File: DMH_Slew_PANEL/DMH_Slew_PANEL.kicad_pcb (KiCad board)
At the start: 2 copper layers, 50 x 200 mm, 5 parts, among them J0 Panel_GND_Solder_Wire_Pad

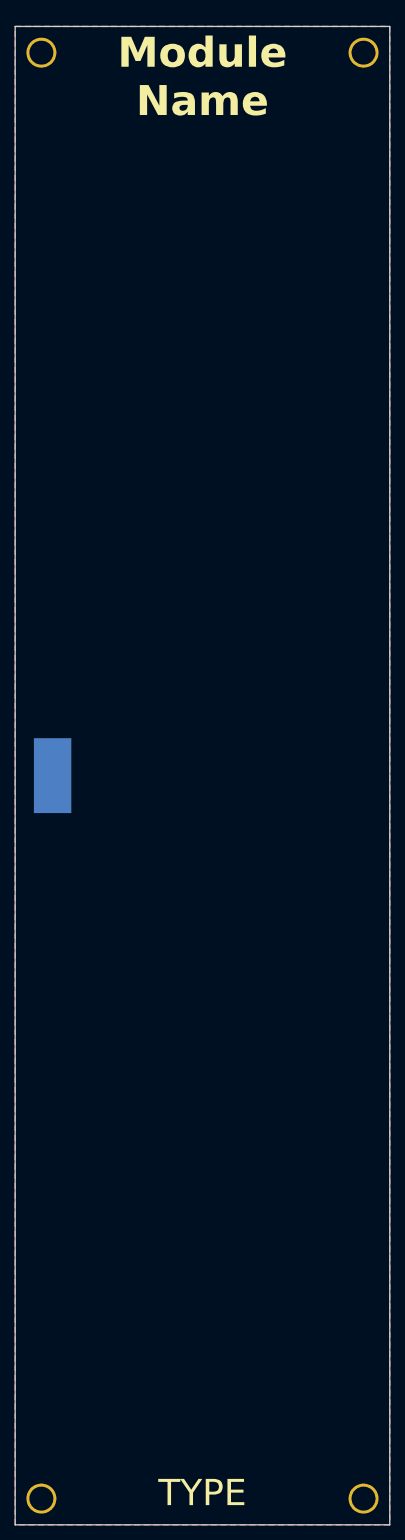
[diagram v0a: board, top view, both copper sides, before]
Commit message: Designed front panel
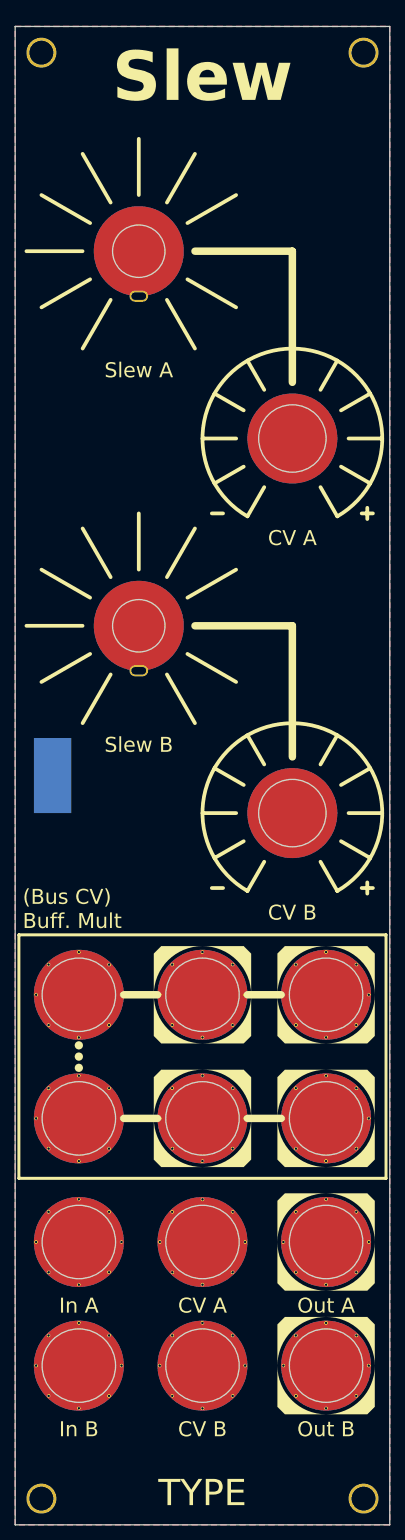
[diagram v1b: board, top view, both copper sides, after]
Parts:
- added H10: Out B, SynthStuff:Jack_6.35mm_Cutout_Output_v6, F.Cu at (91.5, 208.8)
- added H11: Mult In B, SynthStuff:Jack_6.35mm_Cutout_v3, F.Cu at (58.5, 175.8)
- added H12: Mult In A, SynthStuff:Jack_6.35mm_Cutout_v3, F.Cu at (58.5, 159.2)
- added H13: Mult Out A 1, SynthStuff:Jack_6.35mm_Cutout_Output_v6, F.Cu at (75.0, 159.2)
- added H14: Mult Out A 2, SynthStuff:Jack_6.35mm_Cutout_Output_v6, F.Cu at (91.5, 159.2)
- added H15: Mult Out B 1, SynthStuff:Jack_6.35mm_Cutout_Output_v6, F.Cu at (75.0, 175.8)
- added H16: Mult Out B 2, SynthStuff:Jack_6.35mm_Cutout_Output_v6, F.Cu at (91.5, 175.8)
- added H17: Slew A, SynthStuff:Pot_Cutout_Small, F.Cu at (66.5, 60.0)
- added H18: CV A, SynthStuff:Pot_Cutout_Tiny_attv_P110KH1, F.Cu at (87.0, 85.0)
- added H19: Slew B, SynthStuff:Pot_Cutout_Small, F.Cu at (66.5, 110.0)
- added H20: CV B, SynthStuff:Pot_Cutout_Tiny_attv_P110KH1, F.Cu at (87.0, 135.0)
- added H5: In A, SynthStuff:Jack_6.35mm_Cutout_v3, F.Cu at (58.5, 192.2)
- added H6: CV A, SynthStuff:Jack_6.35mm_Cutout_v3, F.Cu at (75.0, 192.2)
- added H7: Out A, SynthStuff:Jack_6.35mm_Cutout_Output_v6, F.Cu at (91.5, 192.2)
- added H8: In B, SynthStuff:Jack_6.35mm_Cutout_v3, F.Cu at (58.5, 208.8)
- added H9: CV B, SynthStuff:Jack_6.35mm_Cutout_v3, F.Cu at (75.0, 208.8)
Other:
- board text added: "(Bus CV) Buff. Mult"
- board text added: "Slew"
- board text removed: "Module Name"

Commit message: Redesign ongoing
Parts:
- removed H11: Mult In B, SynthStuff:Jack_6.35mm_Cutout_v3
- removed J0: Panel_GND_Solder_Wire_Pad, SynthStuff:Panel_GND_SolderWirePad_5x10mm
- added H21: Shape, SynthStuff:Toggle_Switch_TE_Cutout, F.Cu at (91.5, 60.0)
- added H22: Shape, SynthStuff:Toggle_Switch_TE_Cutout, F.Cu at (91.5, 110.0)
- added H23: Mode, SynthStuff:Toggle_Switch_TE_Cutout, F.Cu at (58.5, 175.8)
- H18, H6: value CV A -> CV A [R]
- H20, H9: value CV B -> CV B [F]
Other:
- board text added: "[Fall]"
- board text added: "[Rise]"

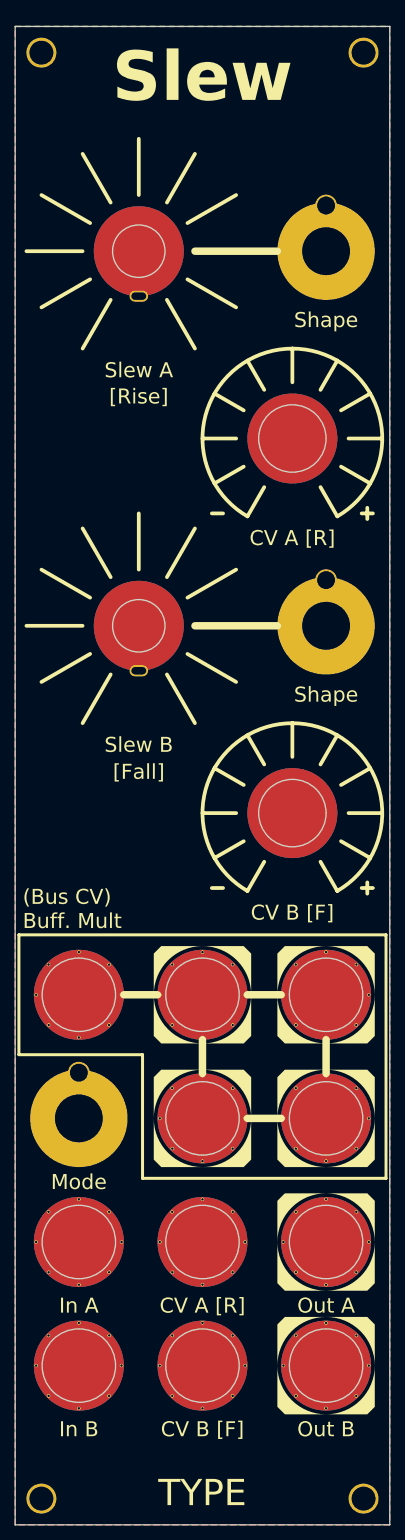
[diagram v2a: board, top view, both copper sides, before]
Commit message: Redesigned front panel
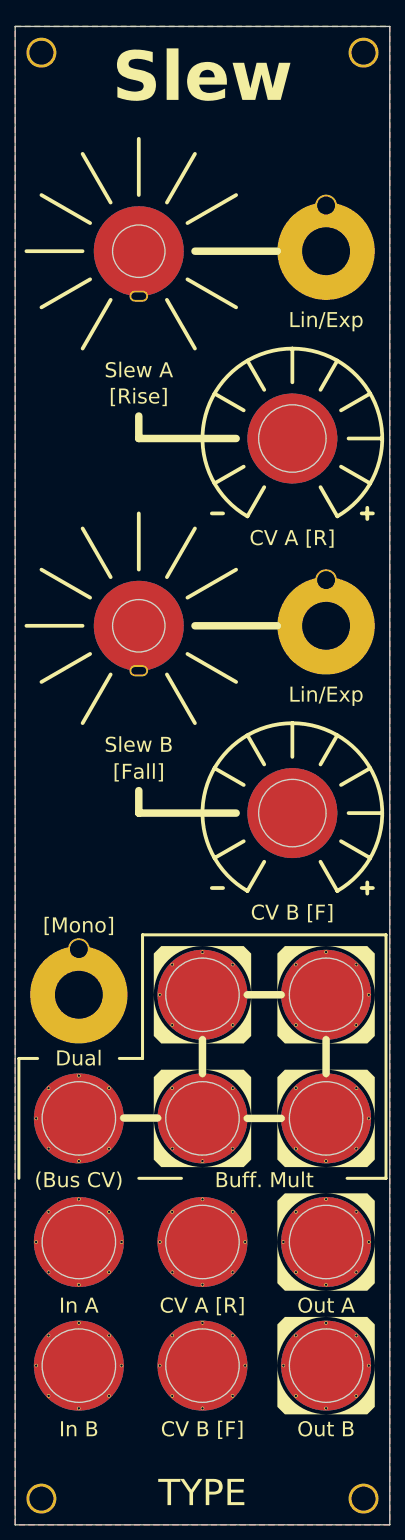
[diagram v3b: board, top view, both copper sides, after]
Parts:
- H21, H22: value Shape -> Lin/Exp
- H23: value Mode -> Dual
- moved H12 16.5 mm to (58.5, 175.8)
- moved H23 16.5 mm to (58.5, 159.2)
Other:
- board text added: "(Bus CV)"
- board text added: "Buff. Mult"
- board text added: "[Mono]"
- board text removed: "(Bus CV) Buff. Mult"

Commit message: Schematic design in progress
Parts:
- H23: value Dual -> A & B
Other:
- board text added: "[R & F]"
- board text removed: "[Mono]"

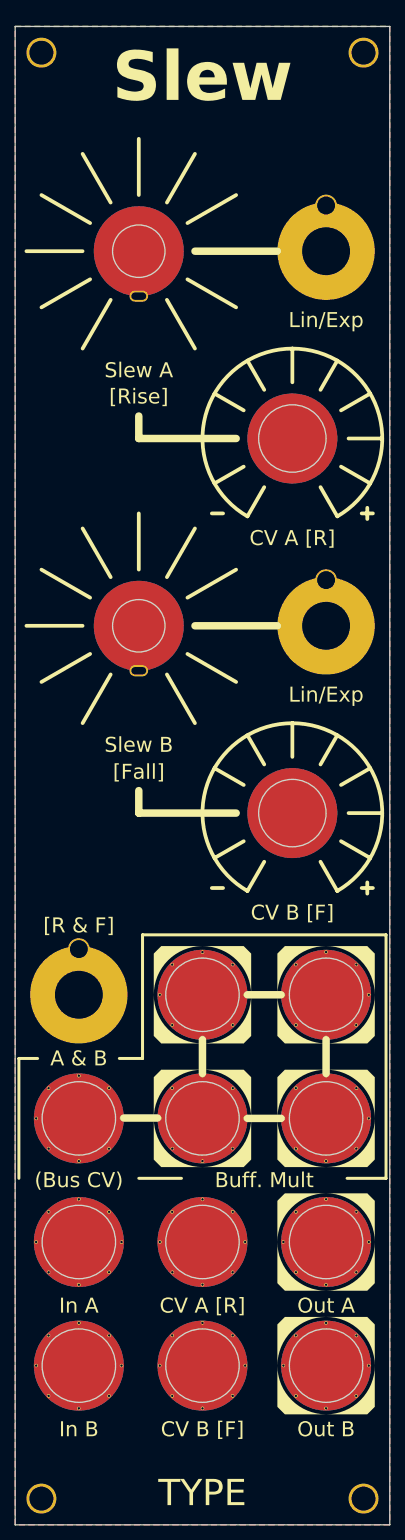
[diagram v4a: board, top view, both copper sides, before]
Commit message: Applied 10V to pots
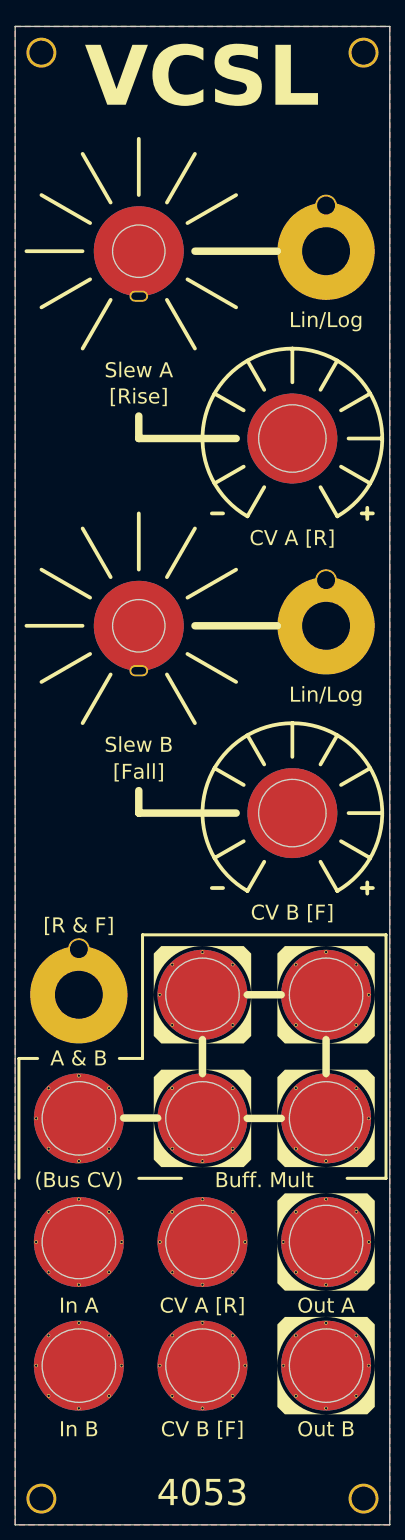
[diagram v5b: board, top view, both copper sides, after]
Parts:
- H21, H22: value Lin/Exp -> Lin/Log
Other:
- board text added: "4053"
- board text added: "VCSL"
- board text removed: "Slew"
- board text removed: "TYPE"
